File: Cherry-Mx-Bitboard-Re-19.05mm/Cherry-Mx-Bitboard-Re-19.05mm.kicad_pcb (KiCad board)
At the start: 2 copper layers, 17.8 x 17.8 mm, 11 parts, among them SW1 SW_Push

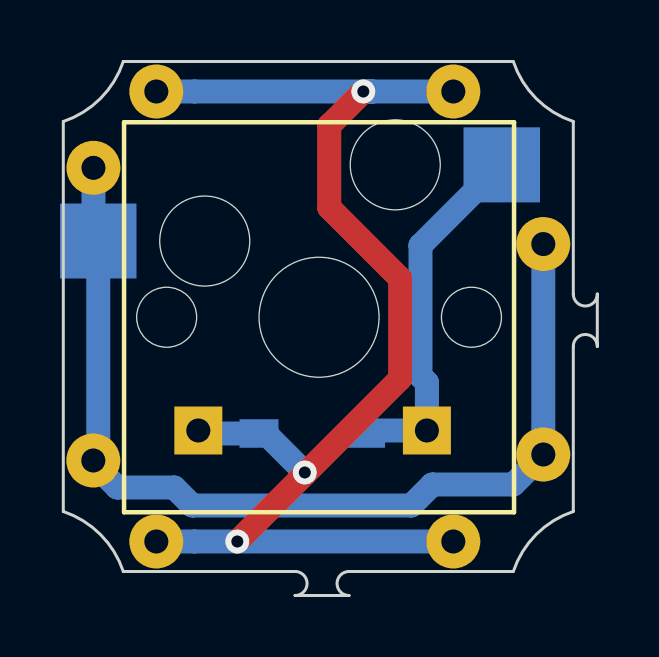
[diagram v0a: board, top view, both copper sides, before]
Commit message: move via next to col
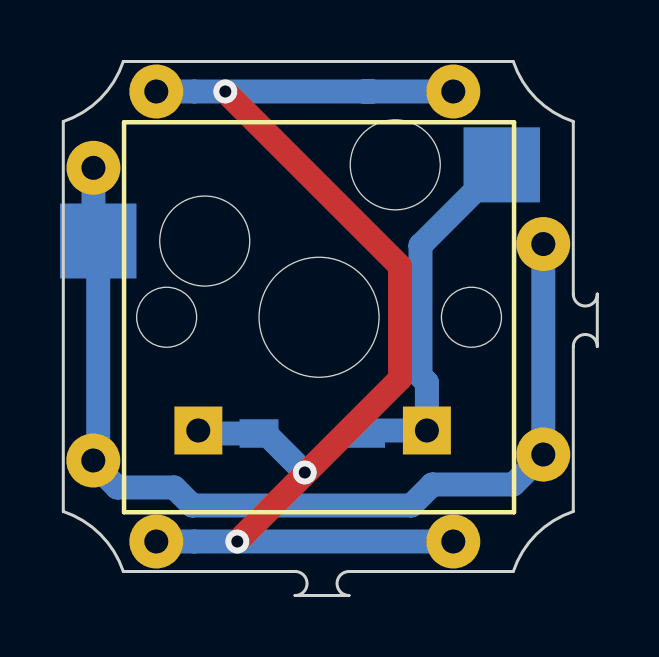
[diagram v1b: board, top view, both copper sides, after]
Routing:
- net Col1: track 43.5 -> 44.5 mm
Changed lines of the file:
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@@
     (thickness 1.6)
     (drawings 22)
-    (tracks 43)
+    (tracks 41)
     (zones 0)
     (modules 11)
@@
   (segment (start 87.245 46.315) (end 88.517792 46.315) (width 0.8) (layer B.Cu) (net 2))
   (segment (start 87.245 61.315) (end 88.517792 61.315) (width 0.8) (layer B.Cu) (net 2))
-  (via (at 94.145 46.315) (size 0.8) (drill 0.4) (layers F.Cu B.Cu) (net 2))
   (segment (start 94.445 46.315) (end 94.145 46.315) (width 0.8) (layer B.Cu) (net 2))
   (segment (start 94.445 46.315) (end 97.345 46.315) (width 0.8) (layer B.Cu) (net 2))
-  (segment (start 88.517792 46.315) (end 94.445 46.315) (width 0.8) (layer B.Cu) (net 2))
-  (segment (start 95.370001 52.543999) (end 95.370001 55.889999) (width 0.8) (layer F.Cu) (net 2))
-  (segment (start 93.009999 50.183997) (end 95.370001 52.543999) (width 0.8) (layer F.Cu) (net 2))
-  (segment (start 94.145 46.315) (end 93.009999 47.450001) (width 0.8) (layer F.Cu) (net 2))
-  (segment (start 93.009999 47.450001) (end 93.009999 50.183997) (width 0.8) (layer F.Cu) (net 2))
   (via (at 89.945 61.315) (size 0.8) (drill 0.4) (layers F.Cu B.Cu) (net 2))
   (segment (start 88.517792 61.315) (end 89.945 61.315) (width 0.8) (layer B.Cu) (net 2))
   (segment (start 89.945 61.315) (end 97.345 61.315) (width 0.8) (layer B.Cu) (net 2))
   (segment (start 90.67 57.715) (end 90.845 57.715) (width 0.8) (layer B.Cu) (net 2))
-  (segment (start 95.370001 55.889999) (end 92.195 59.065) (width 0.8) (layer F.Cu) (net 2))
   (segment (start 88.745 57.715) (end 88.645 57.615) (width 0.8) (layer B.Cu) (net 2))
   (segment (start 90.67 57.715) (end 88.745 57.715) (width 0.8) (layer B.Cu) (net 2))
-  (segment (start 92.195 59.065) (end 89.945 61.315) (width 0.8) (layer F.Cu) (net 2))
   (via (at 92.195 59.015) (size 0.8) (drill 0.4) (layers F.Cu B.Cu) (net 2))
   (segment (start 90.67 57.715) (end 90.895 57.715) (width 0.8) (layer B.Cu) (net 2))
   (segment (start 90.895 57.715) (end 92.195 59.015) (width 0.8) (layer B.Cu) (net 2))
+  (via (at 89.545 46.315) (size 0.8) (drill 0.4) (layers F.Cu B.Cu) (net 2))
+  (segment (start 95.370001 52.140001) (end 89.545 46.315) (width 0.8) (layer F.Cu) (net 2))
+  (segment (start 95.370001 55.889999) (end 95.370001 52.140001) (width 0.8) (layer F.Cu) (net 2))
+  (segment (start 89.945 61.315) (end 95.370001 55.889999) (width 0.8) (layer F.Cu) (net 2))
+  (segment (start 88.517792 46.315) (end 89.545 46.315) (width 0.8) (layer B.Cu) (net 2))
+  (segment (start 89.545 46.315) (end 94.445 46.315) (width 0.8) (layer B.Cu) (net 2))
   (segment (start 85.15 51.14) (end 85.41 51.4) (width 0.3) (layer B.Cu) (net 3) (status 30))
   (segment (start 85.15 51.66) (end 85.41 51.4) (width 0.3) (layer B.Cu) (net 3) (status 30))

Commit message: fix typo in ProtoCases.com
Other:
- board text added: "ProtoCases.com"
- board text removed: "Protocases.com"
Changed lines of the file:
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@@
     (effects (font (size 1 1) (thickness 0.15)) (justify mirror))
   )
-  (gr_text Protocases.com (at 92.245 59.715) (layer B.SilkS)
+  (gr_text ProtoCases.com (at 92.245 59.715) (layer B.SilkS)
     (effects (font (size 1 1) (thickness 0.15)) (justify mirror))
   )
